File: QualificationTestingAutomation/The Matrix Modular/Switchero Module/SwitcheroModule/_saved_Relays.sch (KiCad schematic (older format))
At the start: 13 parts, among them Q1 2N7002DW, U10 TLP3546, U11 TLP3546, U16 INA181, U17 INA181

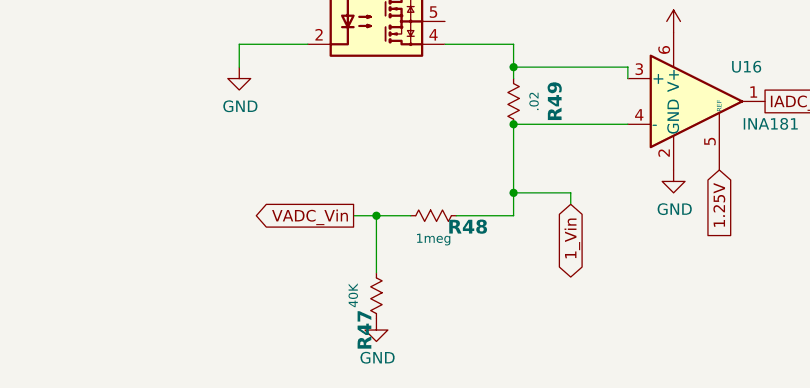
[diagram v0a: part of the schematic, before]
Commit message: Reefero Module PCB design
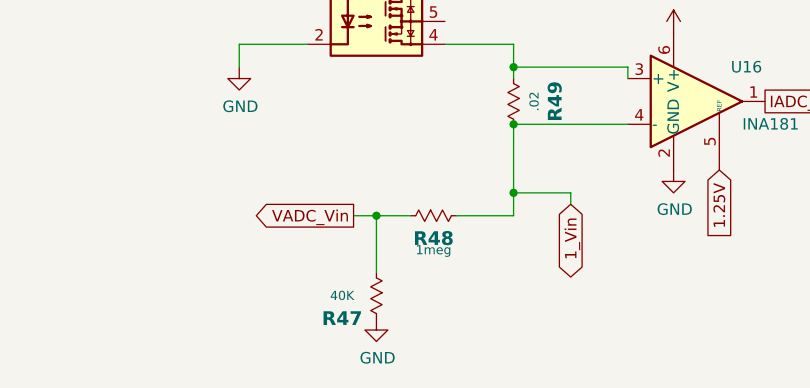
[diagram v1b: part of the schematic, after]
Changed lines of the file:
@@
 AR Path="/5C8DF47A/5CA490DA" Ref="R?"  Part="1"
 AR Path="/5C8DF48C/5CA490DA" Ref="R47"  Part="1"
-F 0 "R47" H 7300 5650 60  0000 C CNB
-F 1 "40K" H 7150 5600 40  0000 C CNN
+F 0 "R47" V 7250 5550 60  0000 C CNB
+F 1 "40K" V 7150 5550 40  0000 C CNN
 F 2 "Resistor_SMD:R_0402_1005Metric" H 7150 5560 40  0001 C CNN
 F 3 "" H 7150 5800 60  0000 C CNN
@@
 AR Path="/5C8DF47A/5CA490E2" Ref="R?"  Part="1"
 AR Path="/5C8DF48C/5CA490E2" Ref="R48"  Part="1"
-F 0 "R48" H 7550 5300 60  0000 C CNB
-F 1 "1meg" H 7400 5250 40  0000 C CNN
+F 0 "R48" H 7400 5250 60  0000 C CNB
+F 1 "1meg" H 7400 5200 40  0000 C CNN
 F 2 "Resistor_SMD:R_0402_1005Metric" H 7400 5210 40  0001 C CNN
 F 3 "" H 7400 5450 60  0000 C CNN
